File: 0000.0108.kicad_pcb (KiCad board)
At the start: 2 copper layers, 130 x 100 mm, 108 parts, among them J1 XA, J10 NC3FAAH, J11 XA, J13 XH, J2 XA, J3 XA, J4 XA, J5 XA, J6 TMT152xx, J7 RAC10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

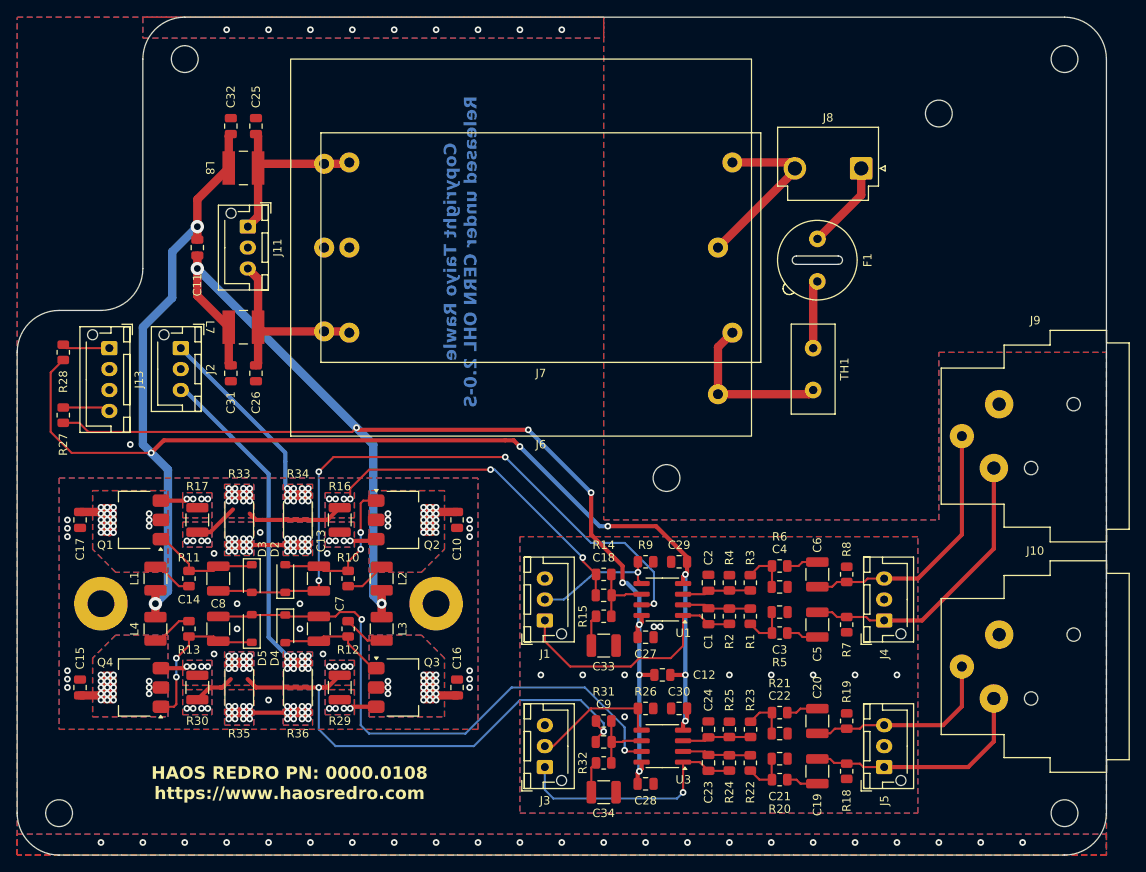
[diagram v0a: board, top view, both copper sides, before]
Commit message: Updated missing or ambiguous component values. Added feed resistor bypass links.
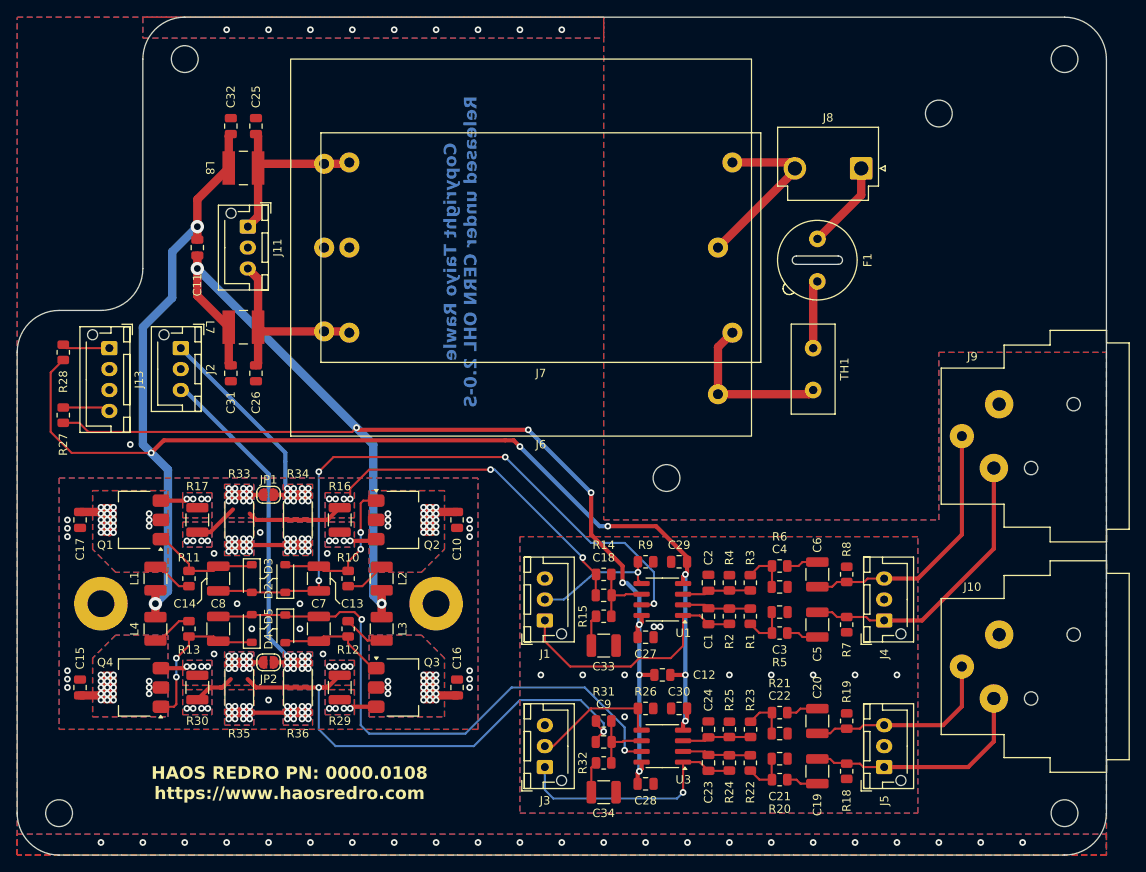
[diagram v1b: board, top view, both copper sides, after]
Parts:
- added JP1: blob, Jumper:SolderJumper-2_P1.3mm_Open_RoundedPad1.0x1.5mm, F.Cu at (125.0, 97.0)
- added JP2: blob, Jumper:SolderJumper-2_P1.3mm_Open_RoundedPad1.0x1.5mm, F.Cu at (125.0, 117.0)
- J1, J11, J2, J3, J4, J5: value XA -> B3B-XH-A
- J13: value XH -> B4B-XH-A
- J6: value TMT152xx -> TMT15215
- J7: value RAC10 -> RAC10-15DK/277
- J8: value JH -> B2P3 -VH
- L1, L2, L3, L4: value 10 -> 10.1210
- L7, L8: value 10 -> 10.4x4
- R14, R31: value 1K -> 3K3
- R26, R9: value 7K5 -> 5K6
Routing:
- net Net-(J2-Pin_3): track 37.3 -> 38.9 mm
- net Net-(J2-Pin_1): track 23.3 -> 24.9 mm
- net /OUT2: track 64.6 -> 66.2 mm
- net /OUT1: track 58.2 -> 59.4 mm

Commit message: Changed XLR input connectors from NC3FAH to NC3FAH2 as the latter is compatible with both. NC3FAH has the shield/screw contact connected to pin 1. NC3FAH2 has this as a separate fourth pin.
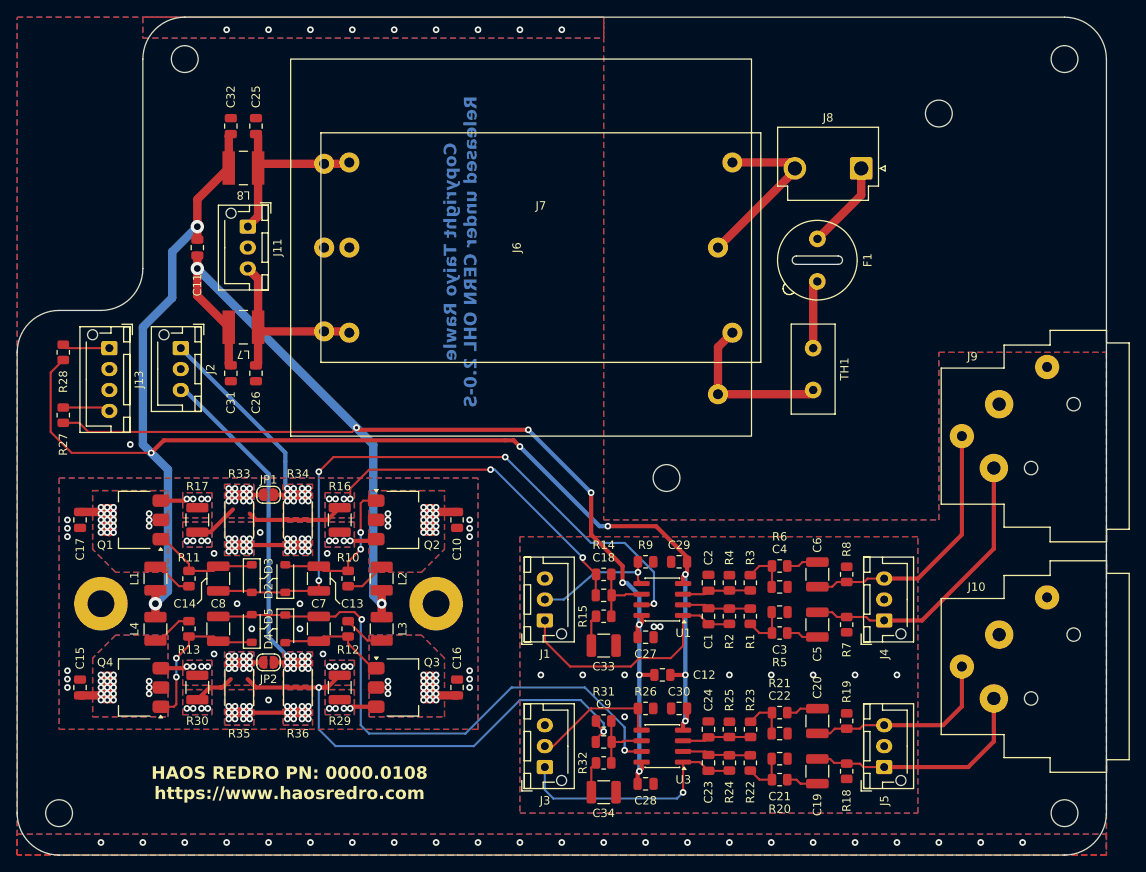
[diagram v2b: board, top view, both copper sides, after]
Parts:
- J10, J9: value NC3FAAH -> NC3FAAH2; footprint Connector_Audio:Jack_XLR_Neutrik_NC3FAAH_Horizontal -> Connector_Audio:Jack_XLR_Neutrik_NC3FAAH2_Horizontal
- J6: footprint HR_Parts:PSU_TRACO_TMT152xx -> HR_parts:PSU_TRACO_TMT152xx
- J7: footprint HR_Parts:RECOM-RAC10 -> HR_parts:RECOM-RAC10
- L7, L8: footprint HR_Parts:INDUCTOR_SMD_4x4 -> HR_parts:INDUCTOR_SMD_4x4
